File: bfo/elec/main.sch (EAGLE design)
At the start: 19 parts, among them Q1 BC108B, Q2 BC108B

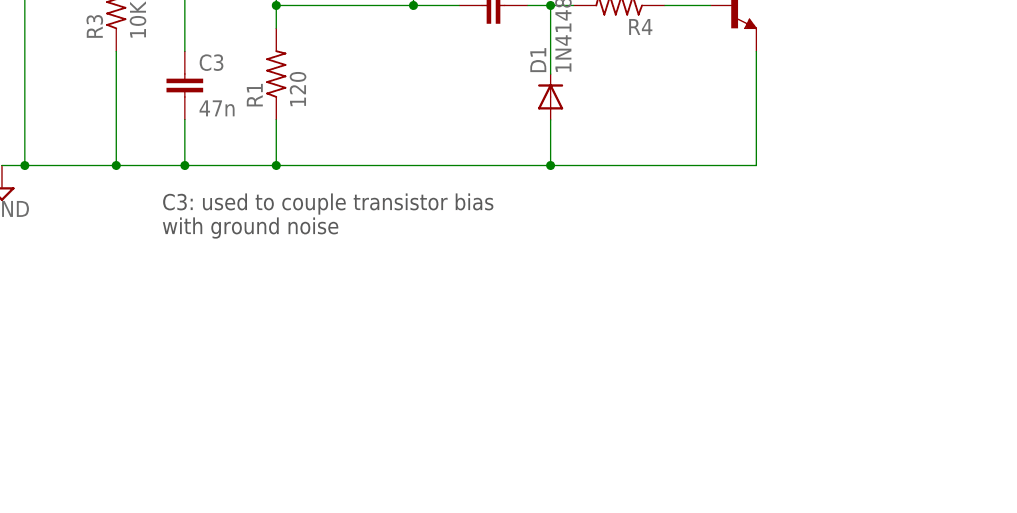
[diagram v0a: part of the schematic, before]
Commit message: bfo/elec: low drift capacitors note
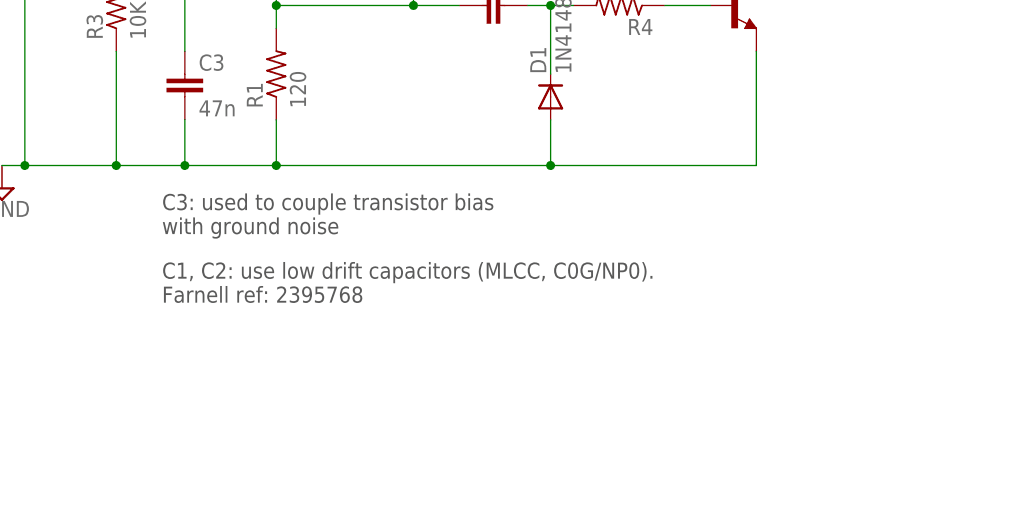
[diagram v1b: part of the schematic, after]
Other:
- note added: "C1, C2: use low drift capacitors (MLCC, C0G/NP0). Farnell ref: 2395768"
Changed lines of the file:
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@@
 <setting verticaltext="up"/>
 </settings>
-<grid distance="0.1" unitdist="inch" unit="inch" style="lines" multiple="1" display="yes" altdistance="0.01" altunitdist="inch" altunit="inch"/>
+<grid distance="0.1" unitdist="inch" unit="inch" style="lines" multiple="1" display="no" altdistance="0.01" altunitdist="inch" altunit="inch"/>
 <layers>
 <layer number="1" name="Top" color="4" fill="1" visible="no" active="no"/>
@@
 <text x="116.84" y="-15.24" size="1.778" layer="97" align="center-right">but_cal</text>
 <text x="116.84" y="-17.78" size="1.778" layer="97" align="center-right">but_cal</text>
+<text x="-2.54" y="-20.32" size="1.778" layer="97">C1, C2: use low drift capacitors (MLCC, C0G/NP0).
+Farnell ref: 2395768</text>
 </plain>
 <instances>
